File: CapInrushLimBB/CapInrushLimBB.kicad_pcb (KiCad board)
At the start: 2 copper layers, 100 x 74.5 mm, 35 parts, among them J1 Screw_Terminal_01x02, J2 Screw_Terminal_01x02, J3 Screw_Terminal_01x02, K1 G5LE-1, Q1 IRF9540N, Q2 Q_PMOS_GDSD, Q3 MPSA42, Q4 MPSA42

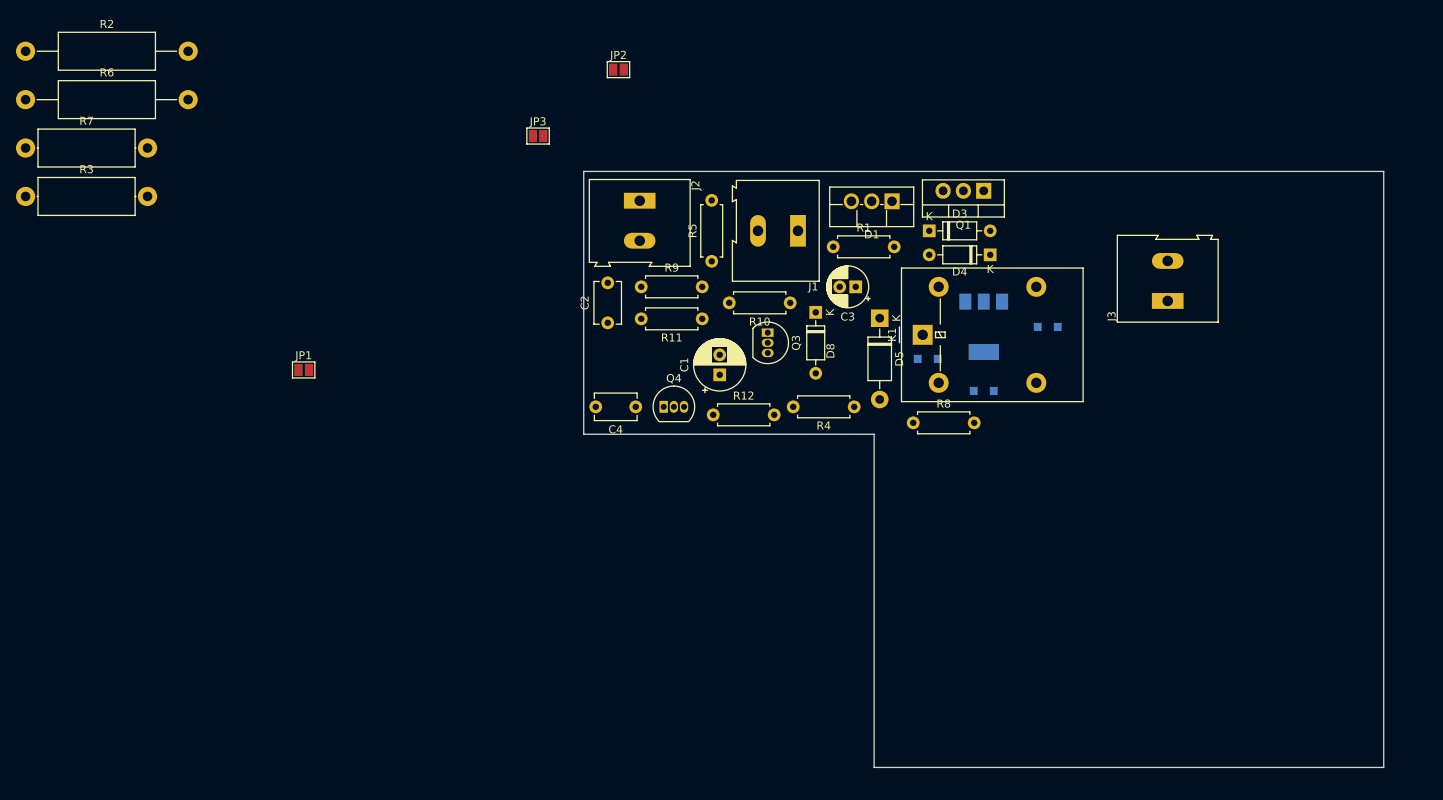
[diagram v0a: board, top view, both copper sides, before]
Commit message: Simplified and labelled schematic and performed work on layout.
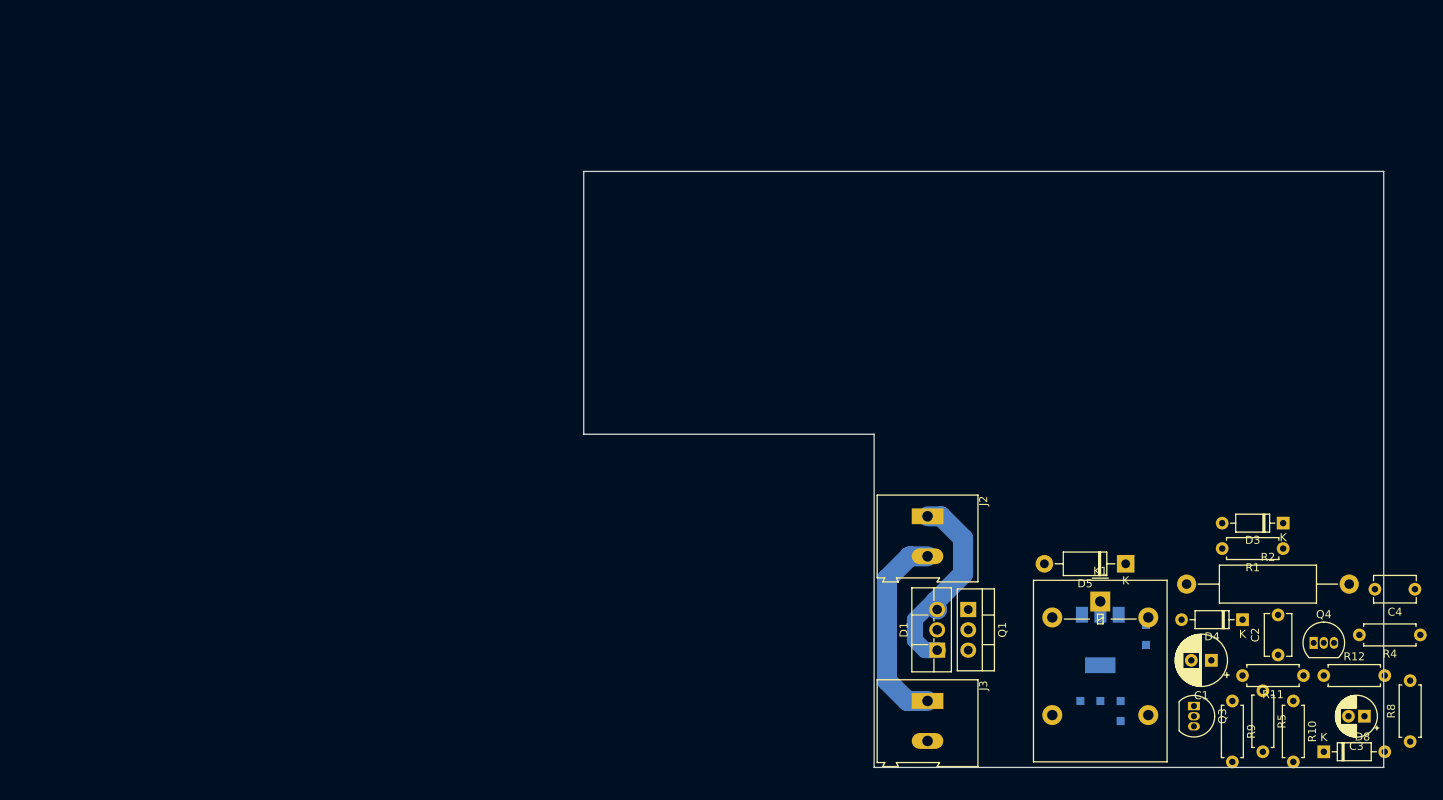
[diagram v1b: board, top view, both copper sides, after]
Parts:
- removed J1: Screw_Terminal_01x02, TerminalBlock:TerminalBlock_Altech_AK300-2_P5.00mm
- removed JP1, JP2, JP3: SolderJumper_2_Open, Jumper:SolderJumper-2_P1.3mm_Open_Pad1.0x1.5mm
- removed R3, R7: 2k2 2W, Resistor_THT:R_Axial_DIN0414_L11.9mm_D4.5mm_P15.24mm_Horizontal
- removed R6: 2k2 2W, Resistor_THT:R_Axial_DIN0414_L11.9mm_D4.5mm_P20.32mm_Horizontal
- moved R2 159.7 mm to (253.4, 137.2)
- moved C4 100.0 mm to (281.9, 137.8)
- moved C2 93.5 mm to (264.8, 146.0)
- moved R9 90.2 mm to (259.1, 151.8), turned to -90 degrees
- moved R11 87.4 mm to (268.0, 148.6)
- moved R5 87.3 mm to (262.9, 150.5), turned to -90 degrees
- moved Q4 86.4 mm to (269.2, 144.5)
- moved D8 84.0 mm to (270.5, 158.1), turned to 0 degrees
- moved C3 83.2 mm to (275.6, 153.7)
- moved R12 83.0 mm to (270.5, 148.6)
- moved R10 80.2 mm to (266.7, 151.8), turned to -90 degrees
- moved R4 76.3 mm to (282.6, 143.5)
- moved R8 73.8 mm to (281.3, 156.8), turned to 90 degrees
- moved C1 71.1 mm to (256.5, 146.7), turned to 180 degrees
- moved Q3 70.8 mm to (254.3, 152.4)
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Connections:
- C2 pad 2: Net-(C2-Pad2) -> /Gnd
- C3 pad 2: Net-(C2-Pad2) -> /Gnd
- C4 pad 2: Net-(C2-Pad2) -> /Gnd
- D1 pad 2: Net-(D1-Pad2) -> /PolProtect
- D3 pad 1: Net-(D1-Pad2) -> /PolProtect
- J2 pad 2: Net-(C2-Pad2) -> /Gnd
- J3 pad 1: /RL_Output -> /Gnd
- J3 pad 2: Net-(C2-Pad2) -> /RL_Output
- K1 pad 5: Net-(JP3-Pad1) -> Net-(K1-Pad5)
- Q1 pad 3: Net-(D1-Pad2) -> /PolProtect
- Q4 pad 1: Net-(C2-Pad2) -> /Gnd
- R1 pad 1: Net-(D1-Pad2) -> /PolProtect
- R10 pad 1: Net-(C2-Pad2) -> /Gnd
- R11 pad 1: Net-(C2-Pad2) -> /Gnd
- R12 pad 1: Net-(C2-Pad2) -> /Gnd
- R2 pad 1: Net-(JP2-Pad1) -> Net-(K1-Pad5)
- R5 pad 2: Net-(J1-Pad2) -> /PolProtect
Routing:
- net /RL_Input: track 0.00 -> 26.1 mm
- net /Gnd: track 0.00 -> 25.1 mm

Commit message: Layout changes.
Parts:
- moved D3 35.8 mm to (236.9, 151.1)
- moved R1 35.8 mm to (236.9, 154.3)
- moved D5 25.3 mm to (268.0, 122.6)
- moved D7 15.6 mm to (244.5, 136.5)
- moved Q2 15.3 mm to (252.7, 132.7)
- moved D6 10.7 mm to (242.6, 142.6)
- moved K1 10.7 mm to (240.0, 128.9)
- moved Q1 5.82 mm to (228.9, 145.4), turned to 90 degrees
- moved D2 3.86 mm to (247.7, 139.7)
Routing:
- net /PolProtect: track 0.00 -> 28.6 mm
- net /RL_Output: track 0.00 -> 27.3 mm
- net /RL_Input: track 26.1 -> 42.1 mm
- net Net-(D3-Pad2): track 0.00 -> 9.02 mm
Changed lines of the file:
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@@
   )
   (footprint "Diode_THT:D_DO-35_SOD27_P7.62mm_Horizontal" (layer "F.Cu")
-    (at 265.43 129.54 180)
+    (at 236.855 151.13 180)
     (descr "Diode, DO-35_SOD27 series, Axial, Horizontal, pin pitch=7.62mm, , length*diameter=4*2mm^2, , http://www.diodes.com/_files/packages/DO-35.pdf")
     (tags "Diode DO-35_SOD27 series Axial Horizontal pin pitch 7.62mm  length 4mm diameter 2mm")
@@
   )
   (footprint "Relay_THT:Relay_SPDT_Omron-G5LE-1" (layer "F.Cu")
-    (at 242.57 139.3275)
+    (at 240.03 128.905)
     (descr "Omron Relay SPDT, http://www.omron.com/ecb/products/pdf/en-g5le.pdf")
     (tags "Omron Relay SPDT")
@@
   )
   (footprint "Diode_THT:D_DO-41_SOD81_P10.16mm_Horizontal" (layer "F.Cu")
-    (at 245.745 134.62 180)
+    (at 267.97 122.555 180)
     (descr "Diode, DO-41_SOD81 series, Axial, Horizontal, pin pitch=10.16mm, , length*diameter=5.2*2.7mm^2, , http://www.diodes.com/_files/packages/DO-41%20(Plastic).pdf")
     (tags "Diode DO-41_SOD81 series Axial Horizontal pin pitch 10.16mm  length 5.2mm diameter 2.7mm")
@@
   )
   (footprint "Resistor_THT:R_Axial_DIN0207_L6.3mm_D2.5mm_P7.62mm_Horizontal" (layer "F.Cu")
-    (at 265.43 132.715 180)
+    (at 236.855 154.305 180)
     (descr "Resistor, Axial_DIN0207 series, Axial, Horizontal, pin pitch=7.62mm, 0.25W = 1/4W, length*diameter=6.3*2.5mm^2, http://cdn-reichelt.de/documents/datenblatt/B400/1_4W%23YAG.pdf")
     (tags "Resistor Axial_DIN0207 series Axial Horizontal pin pitch 7.62mm 0.25W = 1/4W length 6.3mm diameter 2.5mm")
@@
   )
   (footprint "Package_TO_SOT_THT:TO-220-3_Vertical" (layer "F.Cu")
-    (at 226.0675 140.335 -90)
+    (at 228.91 145.415 90)
     (descr "TO-220-3, Vertical, RM 2.54mm, see https://www.vishay.com/docs/66542/to-220-1.pdf")
     (tags "TO-220-3 Vertical RM 2.54mm")
@@
     (fp_line (start 0.69 -3.15) (end 0.69 -1.88) (layer "F.Fab") (width 0.1))
     (fp_line (start -2.46 1.25) (end 7.54 1.25) (layer "F.Fab") (width 0.1))
-    (pad "1" thru_hole rect (at 0 0 270) (size 1.905 2) (drill 1.1) (layers *.Cu *.Mask)
+    (pad "1" thru_hole rect (at 0 0 90) (size 1.905 2) (drill 1.1) (layers *.Cu *.Mask)
       (net 8 "Net-(D3-Pad2)") (pinfunction "G") (pintype "input"))
-    (pad "2" thru_hole oval (at 2.54 0 270) (size 1.905 2) (drill 1.1) (layers *.Cu *.Mask)
+    (pad "2" thru_hole oval (at 2.54 0 90) (size 1.905 2) (drill 1.1) (layers *.Cu *.Mask)
       (net 1 "/RL_Output") (pinfunction "D") (pintype "passive"))
-    (pad "3" thru_hole oval (at 5.08 0 270) (size 1.905 2) (drill 1.1) (layers *.Cu *.Mask)
+    (pad "3" thru_hole oval (at 5.08 0 90) (size 1.905 2) (drill 1.1) (layers *.Cu *.Mask)
       (net 17 "/PolProtect") (pinfunction "S") (pintype "passive"))
     (model "${KICAD6_3DMODEL_DIR}/Package_TO_SOT_THT.3dshapes/TO-220-3_Vertical.wrl"
@@
   )
   (footprint "Diode_SMD:D_SOD-323_HandSoldering" (layer "B.Cu")
-    (at 245.11 153.035 -90)
+    (at 242.57 142.6125 -90)
     (descr "SOD-323")
     (tags "SOD-323")
@@
   )
   (footprint "Package_TO_SOT_SMD:SOT-223" (layer "B.Cu")
-    (at 242.57 144.145 -90)
+    (at 252.73 132.715 -90)
     (descr "module CMS SOT223 4 pins")
     (tags "CMS SOT")
@@
   )
   (footprint "Diode_SMD:D_SOD-323_HandSoldering" (layer "B.Cu")
-    (at 241.32 151.765 180)
+    (at 244.475 136.525 180)
     (descr "SOD-323")
     (tags "SOD-323")
@@
   )
   (footprint "Diode_SMD:D_SOD-323_HandSoldering" (layer "B.Cu")
-    (at 248.285 143.51 -90)
+    (at 247.65 139.7 -90)
     (descr "SOD-323")
     (tags "SOD-323")
@@
   (gr_line locked (start 278 85.575) (end 278 160.075) (layer "Edge.Cuts") (width 0.1))
   (gr_line locked (start 178 118.425) (end 214.3 118.425) (layer "Edge.Cuts") (width 0.1))
-  (segment (start 222.183 140.335) (end 221.9325 140.0845) (width 2.5) (layer "B.Cu") (net 6))
+  (segment (start 228.91 142.875) (end 233.8 142.875) (width 2.2) (layer "B.Cu") (net 1))
+  (segment (start 227.33 142.875) (end 228.91 142.875) (width 2.2) (layer "B.Cu") (net 1))
+  (segment (start 225.425 154.52) (end 225.425 156.21) (width 2.2) (layer "B.Cu") (net 1))
+  (segment (start 233.8 142.875) (end 234.03 143.105) (width 2.2) (layer "B.Cu") (net 1))
+  (segment (start 220.98 156.765) (end 227.33 156.765) (width 2.2) (layer "B.Cu") (net 1))
+  (segment (start 225.425 154.52) (end 225.425 144.78) (width 2.2) (layer "B.Cu") (net 1))
+  (segment (start 225.425 144.78) (end 227.33 142.875) (width 2.2) (layer "B.Cu") (net 1))
   (segment (start 222.31 145.415) (end 220.6625 145.415) (width 2) (layer "B.Cu") (net 6))
-  (segment (start 225.425 135.89) (end 221.9325 139.3825) (width 2.5) (layer "B.Cu") (net 6))
-  (segment (start 221.9325 140.0845) (end 221.9325 139.3825) (width 2.5) (layer "B.Cu") (net 6))
+  (segment (start 221.9325 139.3825) (end 225.425 135.89) (width 2.5) (layer "B.Cu") (net 6))
+  (segment (start 226.224511 128.105489) (end 239.230489 128.105489) (width 2.5) (layer "B.Cu") (net 6))
+  (segment (start 239.230489 128.105489) (end 240.03 128.905) (width 2.5) (layer "B.Cu") (net 6))
+  (segment (start 222.183 140.335) (end 221.9325 140.0845) (width 2.2) (layer "B.Cu") (net 6))
   (segment (start 220.6625 145.415) (end 219.3925 144.145) (width 2) (layer "B.Cu") (net 6))
-  (segment (start 225.425 131.445) (end 225.425 135.89) (width 2.5) (layer "B.Cu") (net 6))
-  (segment (start 220.98 128.68) (end 222.66 128.68) (width 2.5) (layer "B.Cu") (net 6))
-  (segment (start 222.66 128.68) (end 225.425 131.445) (width 2.5) (layer "B.Cu") (net 6))
+  (segment (start 225.425 128.905) (end 225.2 128.68) (width 2.5) (layer "B.Cu") (net 6))
+  (segment (start 225.2 128.68) (end 220.98 128.68) (width 2.5) (layer "B.Cu") (net 6))
   (segment (start 219.3925 141.605) (end 222.25 138.7475) (width 2) (layer "B.Cu") (net 6))
   (segment (start 219.3925 144.145) (end 219.3925 141.605) (width 2) (layer "B.Cu") (net 6))
+  (segment (start 225.425 135.89) (end 225.425 128.905) (width 2.5) (layer "B.Cu") (net 6))
+  (segment (start 225.425 128.905) (end 226.224511 128.105489) (width 2.5) (layer "B.Cu") (net 6))
+  (segment (start 229.235 151.13) (end 229.235 154.305) (width 0.6096) (layer "B.Cu") (net 8))
+  (segment (start 229.235 145.74) (end 228.91 145.415) (width 0.6096) (layer "B.Cu") (net 8))
+  (segment (start 229.235 151.13) (end 229.235 145.74) (width 0.6096) (layer "B.Cu") (net 8))
   (segment (start 215.9 136.525) (end 218.745 133.68) (width 2.5) (layer "B.Cu") (net 14))
   (segment (start 215.9 149.225) (end 215.9 136.525) (width 2.5) (layer "B.Cu") (net 14))
@@
   (segment (start 218.745 133.68) (end 220.98 133.68) (width 2.5) (layer "B.Cu") (net 14))
   (segment (start 218.44 151.765) (end 215.9 149.225) (width 2.5) (layer "B.Cu") (net 14))
+  (segment (start 234.978691 140.335) (end 228.91 140.335) (width 2.2) (layer "B.Cu") (net 17))
+  (segment (start 236.855 154.305) (end 236.855 151.13) (width 2.2) (layer "B.Cu") (net 17))
+  (segment (start 223.52 142.875) (end 226.06 140.335) (width 2.2) (layer "B.Cu") (net 17))
+  (segment (start 236.855 151.13) (end 236.855 142.211309) (width 2.2) (layer "B.Cu") (net 17))
+  (segment (start 226.06 140.335) (end 228.91 140.335) (width 2.2) (layer "B.Cu") (net 17))
+  (segment (start 236.855 142.211309) (end 234.978691 140.335) (width 2.2) (layer "B.Cu") (net 17))
+  (segment (start 222.183 142.875) (end 223.52 142.875) (width 2.2) (layer "B.Cu") (net 17))
 )

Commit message: Layout changes.
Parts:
- R9: footprint Resistor_THT:R_Axial_DIN0207_L6.3mm_D2.5mm_P7.62mm_Horizontal -> Resistor_THT:R_Axial_DIN0207_L6.3mm_D2.5mm_P2.54mm_Vertical
- moved D4 22.8 mm to (239.4, 150.5), turned to 0 degrees
- moved R5 16.2 mm to (247.0, 153.7), turned to 180 degrees
- moved C1 11.8 mm to (251.5, 157.4), turned to 90 degrees
- moved R11 7.96 mm to (264.2, 155.6)
- moved D1 5.45 mm to (219.7, 140.6), turned to 0 degrees
- moved R9 3.59 mm to (255.9, 150.1)
- moved Q1 3.48 mm to (225.4, 145.4), turned to 180 degrees
- moved K1 3.20 mm to (236.9, 128.5)
- moved Q3 3.09 mm to (251.5, 151.1), turned to 90 degrees
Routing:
- net /RL_Output: track 27.3 -> 56.7 mm
- net Net-(D3-Pad2): track 9.02 -> 34.4 mm
- net Net-(R10-Pad2): track 0.00 -> 9.32 mm
- net /PolProtect: track 28.6 -> 35.4 mm
- net /RL_Input: track 42.1 -> 36.6 mm
- net Net-(C2-Pad1): track 0.00 -> 4.54 mm

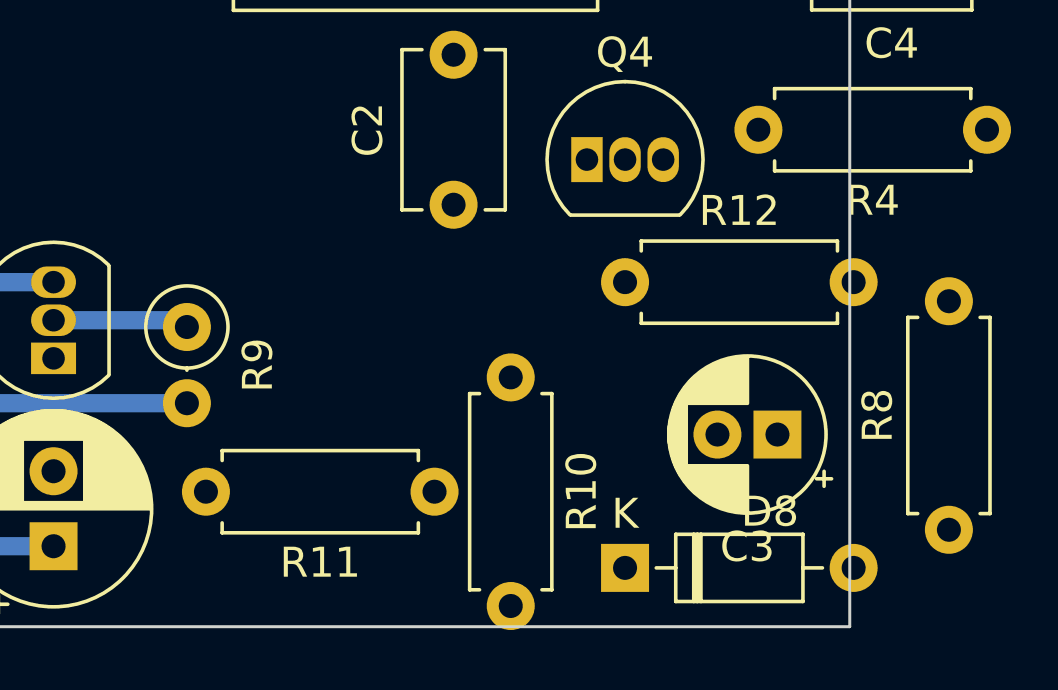
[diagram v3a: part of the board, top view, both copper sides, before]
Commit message: Added new current limiting relay timer.
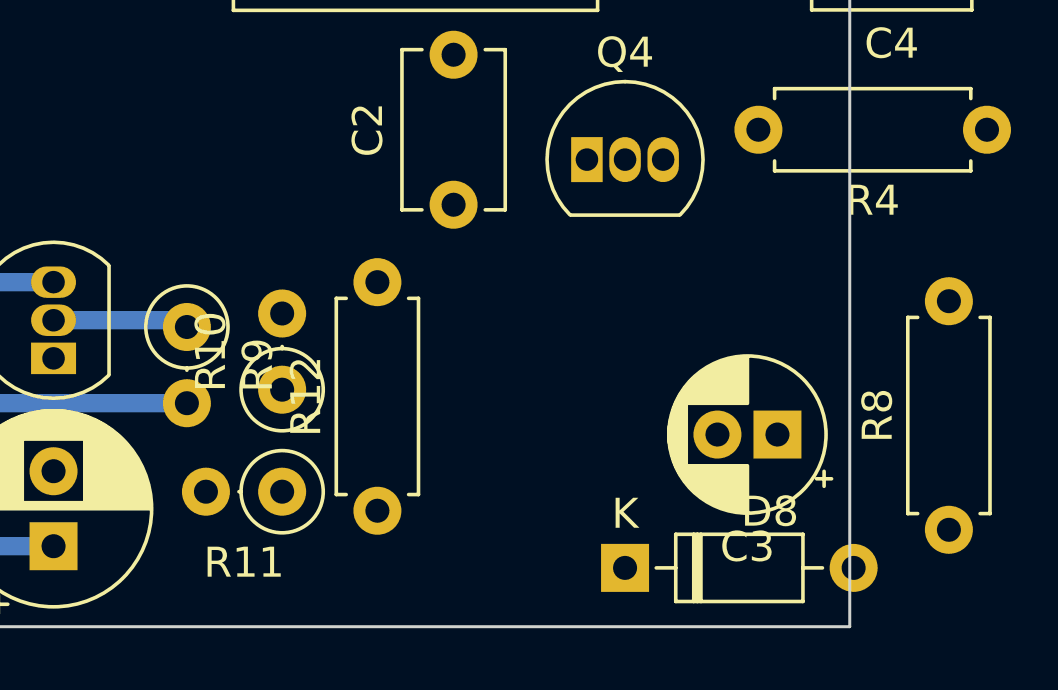
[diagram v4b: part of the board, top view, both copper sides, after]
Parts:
- R10, R11: footprint Resistor_THT:R_Axial_DIN0207_L6.3mm_D2.5mm_P7.62mm_Horizontal -> Resistor_THT:R_Axial_DIN0207_L6.3mm_D2.5mm_P2.54mm_Vertical
- moved R12 11.2 mm to (262.3, 156.2), turned to 90 degrees
- moved R10 7.63 mm to (259.1, 152.2), turned to 90 degrees
- moved R11 5.08 mm to (259.1, 155.6)
